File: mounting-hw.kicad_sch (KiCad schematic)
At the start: 27 parts, among them J1 Conn_01x04, J2 Conn_01x08

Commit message: More scripts to draw border and place footprint
M  drawborder.py
M  mounting-hw.kicad_sch
M  optical-keyboard-mx.kicad_pcb
M  optical-keyboard-mx.kicad_sch
M  placefp.py
 D placefpg.mx
M  placeholes.py
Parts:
- removed J2: Conn_01x08, MyFootprints:PinHeader_1x08_P2.54mm_Vertical, symbol MySymbols:Conn_01x08
- added J10, J11, J12, J13, J14, J15, J16, J17, J18, J19, J2, J20, J21, J22, J23, J24, J25, J26, J27, J28, J29, J3, J30, J4, J5, J6, J7, J8, J9: Conn_01x04, MyFootprints:PinHeader_1x04_P2.54mm_Vertical, symbol MySymbols:Conn_01x04
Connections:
- no-connect marks 12 -> 120

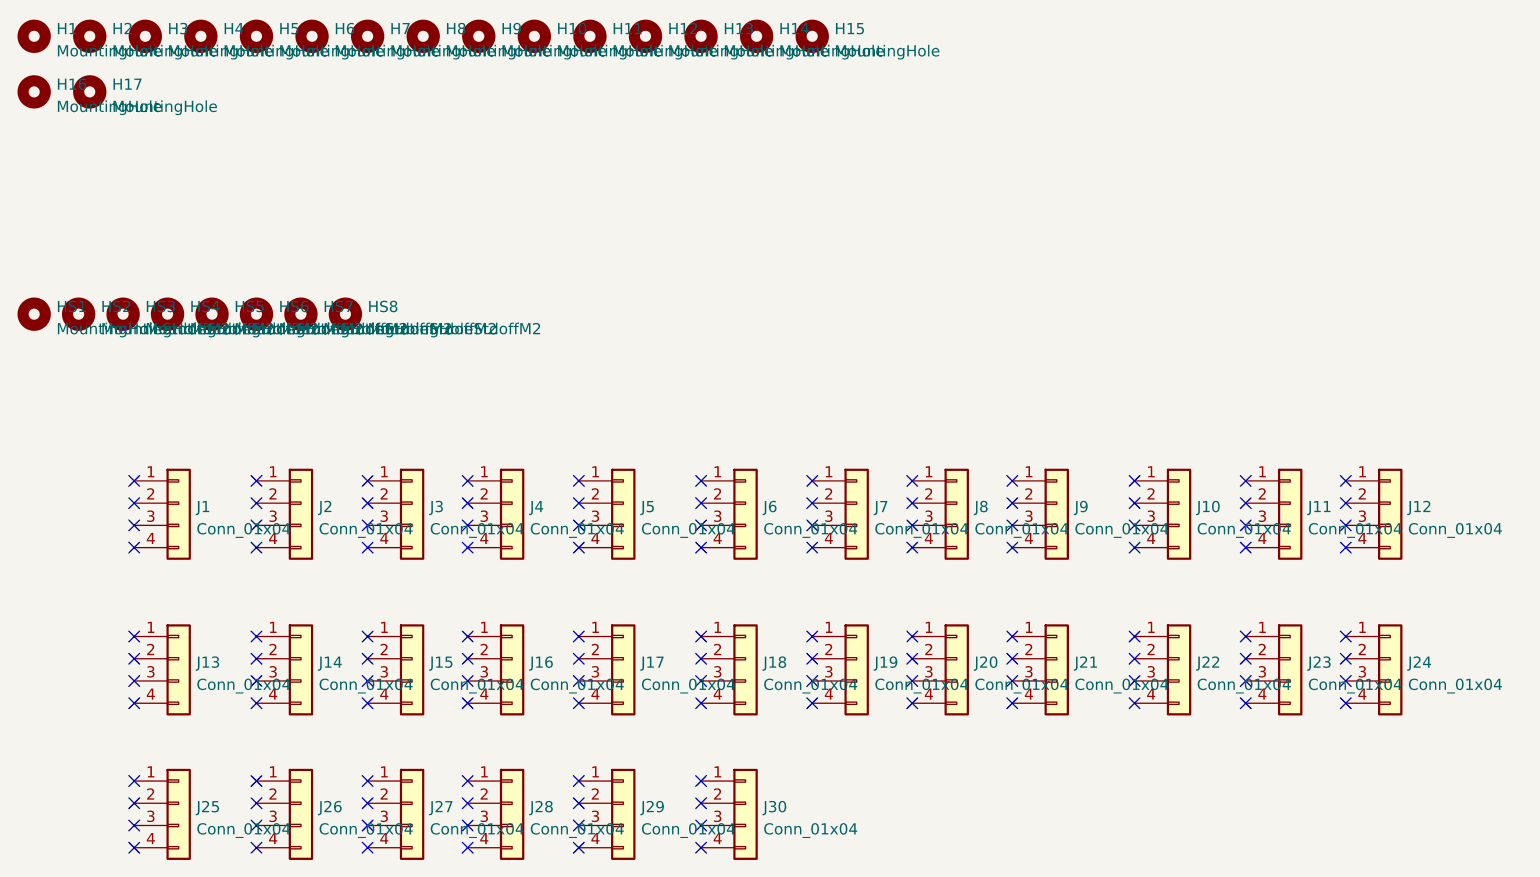
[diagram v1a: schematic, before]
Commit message: Tracks laid, wrist support and switch plate
M  MyFootprints.pretty/BlackPill_STLINK_Down.kicad_mod
M  MyFootprints.pretty/SMTSO_M1.6.kicad_mod
M  MyFootprints.pretty/SMTSO_M2.kicad_mod
M  MyFootprints.pretty/Switch_Cutout.kicad_mod
D  MyFootprints.pretty/Switch_Cutout_1.25u.kicad_mod
D  MyFootprints.pretty/Switch_Cutout_1.5u.kicad_mod
D  MyFootprints.pretty/Switch_Cutout_1.75u.kicad_mod
M  MySymbols.kicad_sym
M  drawborder.py
M  led_driver.kicad_sch
M  mounting-hw.kicad_sch
M  optical-keyboard-mx.kicad_pcb
M  optical-keyboard-mx.kicad_prl
M  optical-keyboard-mx.kicad_pro
M  optical-keyboard-mx.kicad_sch
M  placefp.py
 D placefpg.mx
M  placeholes.py
A  switch-plate/.gitignore
A  switch-plate/fp-lib-table
A  switch-plate/switch-plate.kicad_pcb
A  switch-plate/switch-plate.kicad_prl
A  switch-plate/switch-plate.kicad_pro
A  switch-plate/switch-plate.kicad_sch
A  switch-plate/sym-lib-table
M  switch.kicad_sch
A  wrist-support/.gitignore
A  wrist-support/fp-lib-table
A  wrist-support/sym-lib-table
A  wrist-support/wrist-support.kicad_pcb
A  wrist-support/wrist-support.kicad_prl
A  wrist-support/wrist-support.kicad_pro
A  wrist-support/wrist-support.kicad_sch
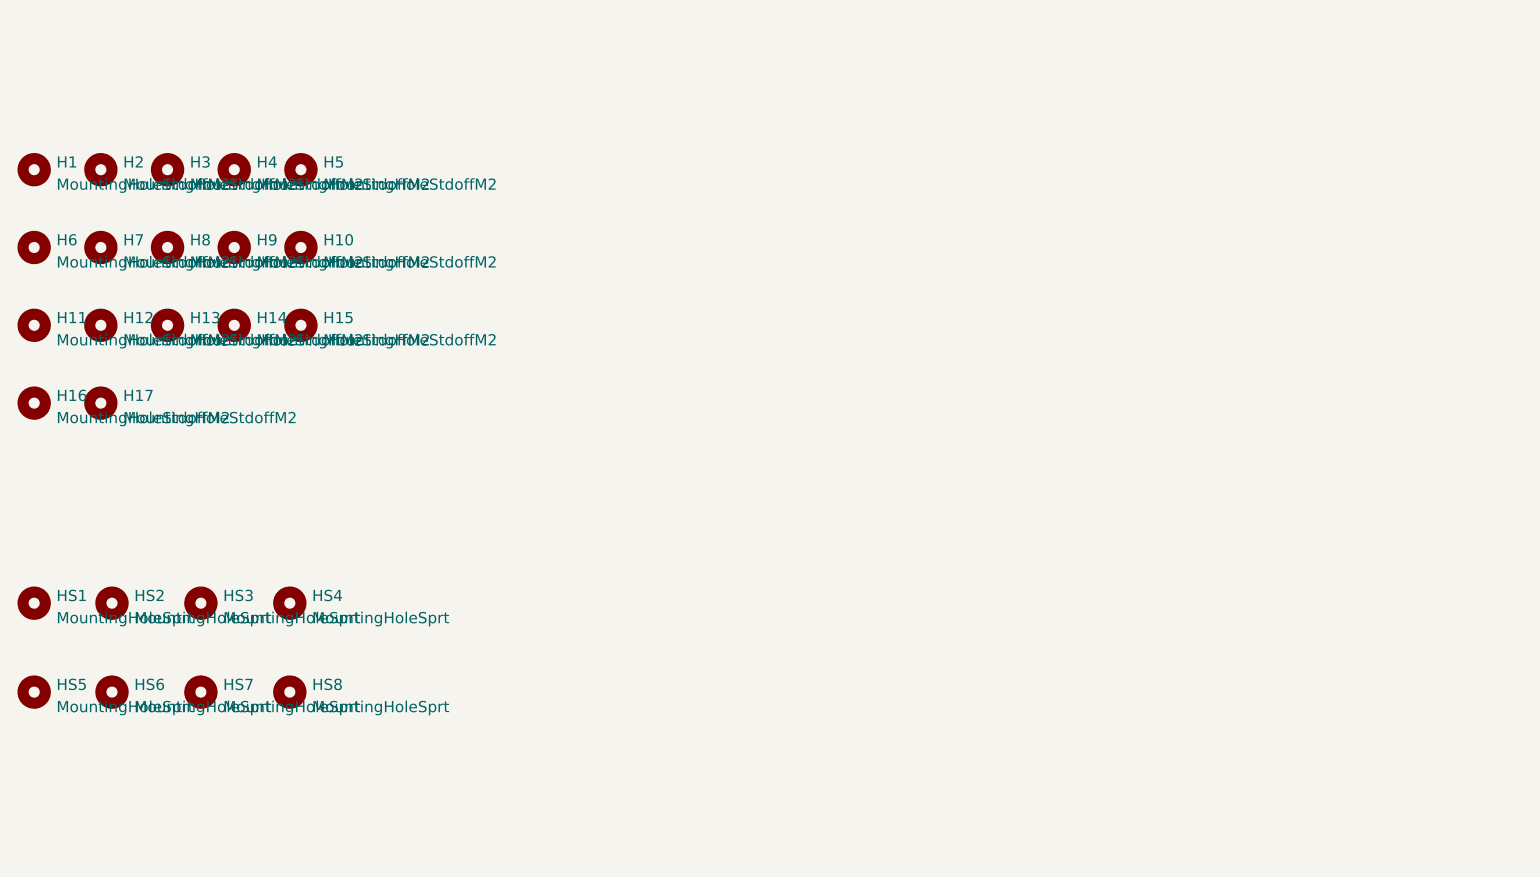
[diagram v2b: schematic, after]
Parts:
- removed H1, H10, H11, H12, H13, H14, H15, H16, H17, H2, H3, H4, H5, H6, H7, H8, H9: MountingHole, MyFootprints:SMTSO_M2, symbol Mechanical:MountingHole
- removed HS1, HS2, HS3, HS4, HS5, HS6, HS7, HS8: MountingHoleStdoffM2, MyFootprints:MountingHole_2.2mm_M2_ISO7380_Pad, symbol MySymbols:MountingHoleStdoffM2
- removed J1, J10, J11, J12, J13, J14, J15, J16, J17, J18, J19, J2, J20, J21, J22, J23, J24, J25, J26, J27, J28, J29, J3, J30, J4, J5, J6, J7, J8, J9: Conn_01x04, MyFootprints:PinHeader_1x04_P2.54mm_Vertical, symbol MySymbols:Conn_01x04
- added H1, H10, H11, H12, H13, H14, H15, H16, H17, H2, H3, H4, H5, H6, H7, H8, H9: MountingHoleStdoffM2, MyFootprints:SMTSO_M2, symbol MySymbols:MountingHoleStdoffM2
- added HS1, HS2, HS3, HS4, HS5, HS6, HS7, HS8: MountingHoleSprt, MyFootprints:SMTSO_M2, symbol MySymbols:MountingHoleSprt
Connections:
- no-connect marks 120 -> 0
